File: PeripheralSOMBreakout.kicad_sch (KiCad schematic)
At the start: 0 parts

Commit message: basic stuff
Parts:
- added J1: 53307-2471, UTSVT_Connectors:PeripheralSOM, symbol utsvt_connectors:PeripheralSOMConnector
- added J2: 24V, Banana:5754, symbol Connector_Generic:Conn_01x01
- added J3: GND, Banana:5754, symbol Connector_Generic:Conn_01x01
- added J4: Digital A, UTSVT_Connectors:CONN_SFH11-xxxC-D05-ST-XX_SUL, symbol utsvt_connectors:SFH11-PBPC-D05-ST-BK
- added J5: Digital B, UTSVT_Connectors:CONN_SFH11-xxxC-D05-ST-XX_SUL, symbol utsvt_connectors:SFH11-PBPC-D05-ST-BK
- added J6: Analog, Connector_PinHeader_2.54mm:PinHeader_1x05_P2.54mm_Vertical, symbol Connector_Generic:Conn_01x05
- added LOGO1: LHRs Logo, UTSVT_Logos:LHRs_LOGO, symbol utsvt_misc:Logo_Placeholder
- added R1, R2: 10k, Resistor_SMD:R_0603_1608Metric_Pad0.98x0.95mm_HandSolder, symbol Device:R
- added TP1: 3V3, Connector_PinHeader_2.54mm:PinHeader_1x01_P2.54mm_Vertical, symbol Connector:TestPoint
- added TP2: VDDA, Connector_PinHeader_2.54mm:PinHeader_1x01_P2.54mm_Vertical, symbol Connector:TestPoint
- added TP3: GND, Connector_PinHeader_2.54mm:PinHeader_1x01_P2.54mm_Vertical, symbol Connector:TestPoint
- added TP4: GNDA, Connector_PinHeader_2.54mm:PinHeader_1x01_P2.54mm_Vertical, symbol Connector:TestPoint
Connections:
- new net +24V: J1.24 (+24V_In), J2.1 (Pin_1)
- new net +3.3V: J1.2 (+3.3v), R1.1, R2.1, TP1.1
- new net ADC1_IN10: J1.13 (ADC1_IN10), J6.2 (Pin_2)
- new net ADC1_IN11: J1.15 (ADC1_IN11), J6.1 (Pin_1)
- new net ADC1_IN7: J1.9 (ADC1_IN7), J6.4 (Pin_4)
- new net ADC1_IN9: J1.11 (ADC1_IN9), J6.3 (Pin_3)
- new net CAN_H: J1.22 (CAN_H), J4.1 (CH0)
- new net CAN_L: J1.20 (CAN_L), J4.2 (CH1)
- new net GND: J1.1 (GND), J1.3 (GND), J1.5 (GND), J3.1 (Pin_1), J4.10 (GND), J4.9 (GND), J5.10 (GND), J5.9 (GND), TP3.1
- new net GNDA: J1.10 (GNDA), TP4.1
- new net I2C1_SCL: J1.6 (I2C1_SCL), J4.4 (CH3), R2.2
- new net I2C1_SDA: J1.4 (I2C1_SDA), J4.3 (CH2), R1.2
- new net OPAMP1_VINP: J1.7 (OPAMP1_VINP), J6.5 (Pin_5)
- new net SPI1_MISO: J1.21 (SPI1_MISO), J4.5 (CH4)
- new net SPI1_MOSI: J1.17 (SPI1_MOSI), J4.6 (CH5)
- new net SPI1_NSS: J1.19 (SPI1_NSS), J4.8 (CH7)
- new net SPI1_SCK: J1.23 (SPI1_SCK), J4.7 (CH6)
- new net SPI2_MISO: J1.14 (SPI2_MISO), J5.1 (CH0)
- new net SPI2_MOSI: J1.16 (SPI2_MOSI), J5.2 (CH1)
- new net SPI2_NSS: J1.12 (SPI2_NSS), J5.4 (CH3)
- new net SPI2_SCK: J1.18 (SPI2_SCK), J5.3 (CH2)
- new net VDDA: J1.8 (VDDA), TP2.1
- no-connect marks 0 -> 8
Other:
- note added: "Analog Testpoints"
- note added: "Digital Testpoints"
- note added: "I2C Pullups"
- note added: "PSOM"
- note added: "PWR Testpoints"
- note added: "Power"
- company: (none) -> LHRs
- title: (none) -> PeripheralSOM Breakout

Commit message: finished
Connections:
- net CAN_H: now also J4.4 (CH3); no longer J4.1 (CH0)
- net CAN_L: now also J4.3 (CH2); no longer J4.2 (CH1)
- net I2C1_SCL: now also J4.2 (CH1); no longer J4.4 (CH3)
- net I2C1_SDA: now also J4.1 (CH0); no longer J4.3 (CH2)
- net SPI2_MOSI: now also J5.4 (CH3); no longer J5.2 (CH1)
- net SPI2_NSS: now also J5.2 (CH1); no longer J5.4 (CH3)
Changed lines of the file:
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@@
-		)
-	)
-	(label "CAN_H"
-		(at 53.34 24.13 0)
-		(effects
-			(font
-				(size 1.27 1.27)
-			)
-			(justify left bottom)
-		)
-	)
-	(label "SPI2_NSS"
-		(at 53.34 67.31 0)
-		(effects
-			(font
-				(size 1.27 1.27)
-			)
-			(justify left bottom)
 		)
 	)
@@
 		)
 	)
+	(label "I2C1_SDA"
+		(at 53.34 24.13 0)
+		(effects
+			(font
+				(size 1.27 1.27)
+			)
+			(justify left bottom)
+		)
+	)
 	(label "ADC1_IN7"
 		(at 53.34 114.3 0)
@@
 		)
 	)
+	(label "SPI2_MOSI"
+		(at 53.34 67.31 0)
+		(effects
+			(font
+				(size 1.27 1.27)
+			)
+			(justify left bottom)
+		)
+	)
 	(label "ADC1_IN9"
 		(at 53.34 111.76 0)
@@
 		)
 	)
-	(label "I2C1_SCL"
-		(at 53.34 31.75 0)
-		(effects
-			(font
-				(size 1.27 1.27)
-			)
-			(justify left bottom)
-		)
-	)
 	(label "I2C1_SDA"
 		(at 160.02 41.91 180)
@@
 		)
 	)
+	(label "CAN_L"
+		(at 53.34 29.21 0)
+		(effects
+			(font
+				(size 1.27 1.27)
+			)
+			(justify left bottom)
+		)
+	)
 	(label "SPI2_SCK"
 		(at 53.34 64.77 0)
@@
 		)
 	)
-	(label "I2C1_SDA"
-		(at 53.34 29.21 0)
-		(effects
-			(font
-				(size 1.27 1.27)
-			)
-			(justify left bottom)
-		)
-	)
 	(label "ADC1_IN10"
 		(at 53.34 109.22 0)
@@
 		)
 	)
-	(label "SPI2_MOSI"
-		(at 53.34 62.23 0)
-		(effects
-			(font
-				(size 1.27 1.27)
-			)
-			(justify left bottom)
-		)
-	)
 	(label "SPI2_NSS"
 		(at 160.02 63.5 180)
@@
 		)
 	)
+	(label "SPI2_NSS"
+		(at 53.34 62.23 0)
+		(effects
+			(font
+				(size 1.27 1.27)
+			)
+			(justify left bottom)
+		)
+	)
 	(label "SPI1_MOSI"
 		(at 160.02 80.01 180)
@@
 		)
 	)
+	(label "CAN_H"
+		(at 53.34 31.75 0)
+		(effects
+			(font
+				(size 1.27 1.27)
+			)
+			(justify left bottom)
+		)
+	)
 	(label "SPI1_MISO"
 		(at 160.02 82.55 180)
@@
 		)
 	)
-	(label "CAN_L"
+	(label "I2C1_SCL"
 		(at 53.34 26.67 0)
 		(effects

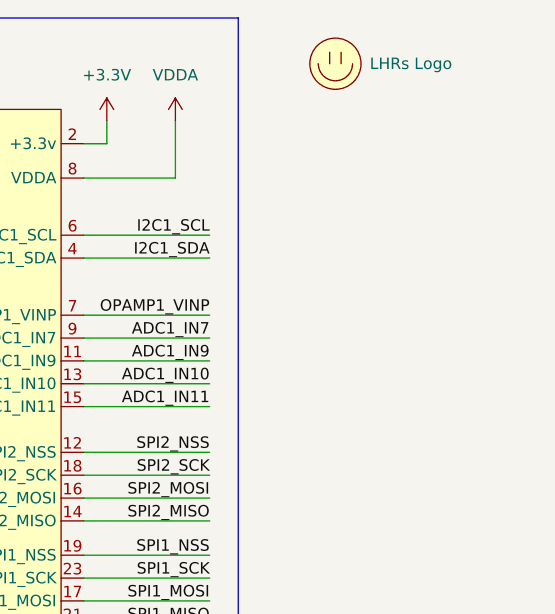
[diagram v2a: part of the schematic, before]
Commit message: add db9 for can
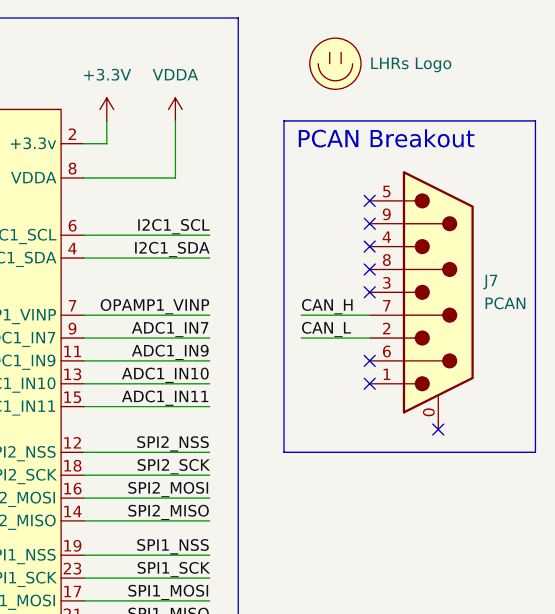
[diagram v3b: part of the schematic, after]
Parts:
- added J7: PCAN, DB9:AMPHENOL_L77SDE09SA4CH3R, symbol Connector:DE9_Pins_MountingHoles
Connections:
- net CAN_H: now also J7.7
- net CAN_L: now also J7.2
- no-connect marks 8 -> 16
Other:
- note added: "PCAN Breakout"
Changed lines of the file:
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@@
+	)
+	(rectangle
+		(start 168.275 26.67)
+		(end 196.215 63.5)
+		(stroke
+			(width 0)
+			(type default)
+		)
+		(fill
+			(type none)
+		)
 	)
 	(rectangle
@@
 		(exclude_from_sim no)
 		(at 25.654 58.928 0)
+		(effects
+			(font
+				(size 1.905 1.905)
+			)
+		)
+	)
+	(text "PCAN Breakout"
+		(exclude_from_sim no)
+		(at 179.578 28.956 0)
 		(effects
 			(font
@@
 	)
 	(no_connect
+		(at 185.42 60.96)
+	)
+	(no_connect
+		(at 177.8 53.34)
+	)
+	(no_connect
 		(at 63.5 77.47)
+	)
+	(no_connect
+		(at 177.8 55.88)
+	)
+	(no_connect
+		(at 177.8 40.64)
+	)
+	(no_connect
+		(at 177.8 43.18)
 	)
 	(no_connect
@@
 	)
 	(no_connect
+		(at 177.8 38.1)
+	)
+	(no_connect
+		(at 177.8 35.56)
+	)
+	(no_connect
+		(at 177.8 45.72)
+	)
+	(no_connect
 		(at 110.49 67.31)
 	)
@@
 	(wire
 		(pts
+			(xy 170.18 48.26) (xy 177.8 48.26)
+		)
+		(stroke
+			(width 0)
+			(type default)
+		)
+	)
+	(wire
+		(pts
 			(xy 29.21 67.31) (xy 29.21 69.85)
 		)
@@
 		(pts
 			(xy 63.5 62.23) (xy 53.34 62.23)
+		)
+		(stroke
+			(width 0)
+			(type default)
+		)
+	)
+	(wire
+		(pts
+			(xy 170.18 50.8) (xy 177.8 50.8)
 		)
 		(stroke
@@
 		)
 	)
+	(label "CAN_H"
+		(at 170.18 48.26 0)
+		(effects
+			(font
+				(size 1.27 1.27)
+			)
+			(justify left bottom)
+		)
+	)
 	(label "ADC1_IN9"
 		(at 53.34 111.76 0)
@@
 	(label "I2C1_SCL"
 		(at 53.34 26.67 0)
+		(effects
+			(font
+				(size 1.27 1.27)
+			)
+			(justify left bottom)
+		)
+	)
+	(label "CAN_L"
+		(at 170.18 50.8 0)
 		(effects
 			(font
@@
 					(unit 1)
 				)
+			)
+		)
+	)
+	(symbol
+		(lib_id "Connector:DE9_Pins_MountingHoles")
+		(at 185.42 45.72 0)
+		(unit 1)
+		(exclude_from_sim no)
+		(in_bom yes)
+		(on_board yes)
+		(dnp no)
+		(fields_autoplaced yes)
+		(property "Reference" "J7"
+			(at 190.5 44.4499 0)
+			(effects
+				(font
+					(size 1.27 1.27)
+				)
+				(justify left)
+			)
+		)
+		(property "Value" "PCAN"
+			(at 190.5 46.9899 0)
+			(effects
+				(font
+					(size 1.27 1.27)
+				)
+				(justify left)
+			)
+		)
+		(property "Footprint" "DB9:AMPHENOL_L77SDE09SA4CH3R"
+			(at 185.42 45.72 0)
+			(effects
+				(font
+					(size 1.27 1.27)
+				)
+				(hide yes)
+			)
+		)
+		(property "Datasheet" "~"
+			(at 185.42 45.72 0)
+			(effects
+				(font
+					(size 1.27 1.27)
+				)
+				(hide yes)
+			)
+		)
+		(property "Description" "9-pin D-SUB connector, pins (male), Mounting Hole"
+			(at 185.42 45.72 0)
+			(effects
+				(font
+					(size 1.27 1.27)
+				)
+				(hide yes)
+			)
+		)
+		(pin "4"
+		)
+		(pin "3"
+		)
+		(pin "7"
+		)
+		(pin "0"
+		)
+		(pin "1"
+		)
+		(pin "6"
+		)
+		(pin "8"
+		)
+		(pin "9"
+		)
+		(pin "2"
+		)
+		(pin "5"
+		)
+		(instances
+			(project ""
+				(path "/68ee5562-682b-4f8e-b74b-e6fad0ef65d0"
+					(reference "J7")
+					(unit 1)
+				)
